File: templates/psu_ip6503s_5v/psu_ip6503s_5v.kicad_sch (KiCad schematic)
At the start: 6 parts, among them U10 IP6503S

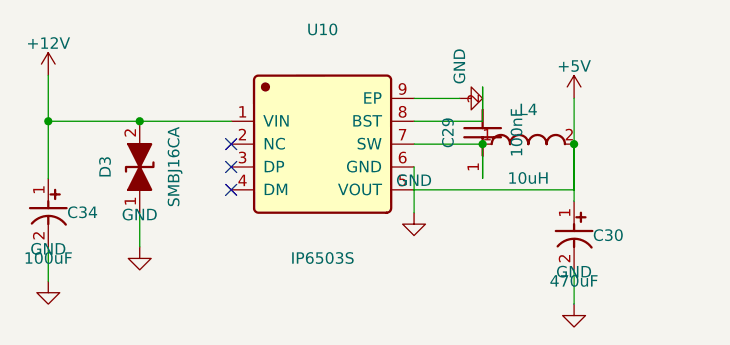
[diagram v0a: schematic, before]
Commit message: Fix IP6503S 5V PSU: upgrade output cap voltage, add ceramic decoupling
Fix #1: Replace C30 output electrolytic from 470uF 6.3V (C2891466) to
470uF 16V (Lelon VZH471M1CTR-0810, C164069). The 6.3V rating had only
26% margin on a 5V rail — now 3.2x derating for reliability.

Fix #2: Add C35 22uF 25V X5R ceramic cap (YAGEO CC1206KKX5R8BB226,
C2178233) in parallel with C30 on the output. Provides low-ESR
high-frequency decoupling for fast load transients that the electrolytic
alone cannot handle.

Both schematic and spec updated. Component count: 6 -> 7.

Co-Authored-By: Claude Opus 4.6 <noreply@anthropic.com>
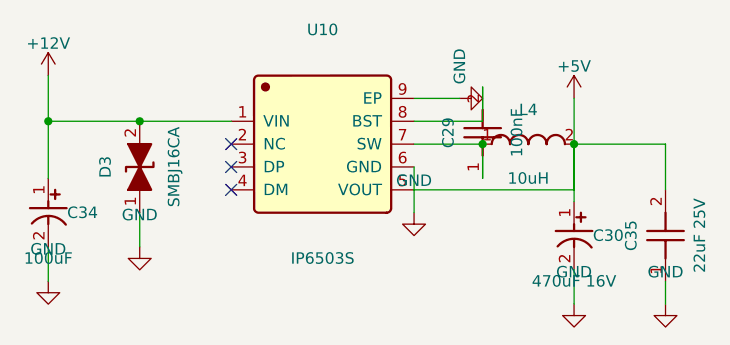
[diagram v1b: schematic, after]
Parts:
- added C35: 22uF 25V, JLCImport:CC1206KKX5R8BB226, symbol JLCImport:CC1206KKX5R8BB226
- C30: value 470uF -> 470uF 16V; footprint JLCImport:EEEFT1V681UP -> JLCImport:VZH471M1CTR-0810; symbol JLCImport:ECAP_470uF_6V3_C2891466 -> JLCImport:ECAP_470uF_16V_C164069; LCSC C2891466 -> C164069
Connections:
- net +5V: now also C35.2
- net GND: now also C35.1
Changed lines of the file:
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@@
+    (stroke (width 0) (type default))
+  )
+  (wire (pts (xy 177.8 100.33) (xy 187.96 100.33))
+    (stroke (width 0) (type default))
+  )
+  (wire (pts (xy 187.96 100.33) (xy 187.96 105.41))
+    (stroke (width 0) (type default))
+  )
+  (wire (pts (xy 187.96 115.57) (xy 187.96 118.11))
     (stroke (width 0) (type default))
   )
@@
   )
   (symbol
-    (lib_id "JLCImport:ECAP_470uF_6V3_C2891466")
+    (lib_id "JLCImport:ECAP_470uF_16V_C164069")
     (at 177.8 110.49 0)
     (unit 1)
@@
       (effects (font (size 1.27 1.27)))
     )
-    (property "Value" "470uF"
+    (property "Value" "470uF 16V"
       (at 177.8 115.57 0)
       (effects (font (size 1.27 1.27)))
     )
-    (property "Footprint" "JLCImport:EEEFT1V681UP"
+    (property "Footprint" "JLCImport:VZH471M1CTR-0810"
       (at 177.8 110.49 0)
       (effects (font (size 1.27 1.27)) hide)
     )
-    (property "LCSC" "C2891466"
+    (property "LCSC" "C164069"
       (at 177.8 110.49 0)
       (effects (font (size 1.27 1.27)) hide)
@@
           (unit 1)
         )
+      )
+    )
+  )
+  (symbol
+    (lib_id "JLCImport:CC1206KKX5R8BB226")
+    (at 187.96 110.49 90)
+    (unit 1)
+    (exclude_from_sim no)
+    (in_bom yes)
+    (on_board yes)
+    (dnp no)
+    (property "Reference" "C35"
+      (at 184.15 110.49 0)
+      (effects (font (size 1.27 1.27)))
+    )
+    (property "Value" "22uF 25V"
+      (at 191.77 110.49 0)
+      (effects (font (size 1.27 1.27)))
+    )
+    (property "Footprint" "JLCImport:CC1206KKX5R8BB226"
+      (at 187.96 110.49 0)
+      (effects (font (size 1.27 1.27)) hide)
+    )
+    (property "LCSC" "C2178233"
+      (at 187.96 110.49 0)
+      (effects (font (size 1.27 1.27)) hide)
+    )
+    (instances
+      (project "AITestProject"
+        (path "/c5e0a3b2-9d4f-6c1a-d7e5-f3a4b6c8d9e0"
+          (reference "C35")
+          (unit 1)
+        )
+      )
+    )
+  )
+  (symbol
+    (lib_id "power:GND")
+    (at 187.96 118.11 0)
+    (unit 1)
+    (exclude_from_sim no)
+    (in_bom yes)
+    (on_board yes)
+    (dnp no)
+    (property "Reference" "#PWR08"
+      (at 187.96 124.46 0)
+      (effects (font (size 1.27 1.27)) hide)
+    )
+    (property "Value" "GND"
+      (at 187.96 114.55 0)
+      (effects (font (size 1.27 1.27)))
+    )
+    (property "Footprint" ""
+      (at 187.96 118.11 0)
+      (effects (font (size 1.27 1.27)) hide)
+    )
+    (instances
+      (project "AITestProject"
+        (path "/c5e0a3b2-9d4f-6c1a-d7e5-f3a4b6c8d9e0"
+          (reference "#PWR08")
+          (unit 1)
+        )

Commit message: Add I2C pullup resistors and apply PSU audit fixes
- R33/R34: 4.22k pullups on SCL/SDA to +3.3V near ESP32
- Fix #2: C108 10uF 35V input cap for U24 3.3V converter
- Fix #3: C3 upgraded from 47uF 16V to 47uF 25V on U1 output
Applied via kicad-patch-tools (non-destructive patching)

Co-Authored-By: Claude Opus 4.6 <noreply@anthropic.com>
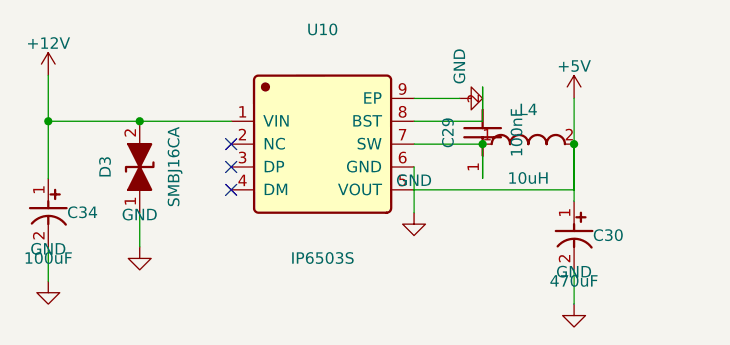
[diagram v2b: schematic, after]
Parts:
- removed C35: 22uF 25V, JLCImport:CC1206KKX5R8BB226, symbol JLCImport:CC1206KKX5R8BB226
- C30: value 470uF 16V -> 470uF; footprint JLCImport:VZH471M1CTR-0810 -> JLCImport:EEEFT1V681UP; symbol JLCImport:ECAP_470uF_16V_C164069 -> JLCImport:ECAP_470uF_6V3_C2891466; LCSC C164069 -> C2891466
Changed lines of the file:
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@@
-    (stroke (width 0) (type default))
-  )
-  (wire (pts (xy 177.8 100.33) (xy 187.96 100.33))
-    (stroke (width 0) (type default))
-  )
-  (wire (pts (xy 187.96 100.33) (xy 187.96 105.41))
-    (stroke (width 0) (type default))
-  )
-  (wire (pts (xy 187.96 115.57) (xy 187.96 118.11))
     (stroke (width 0) (type default))
   )
@@
   )
   (symbol
-    (lib_id "JLCImport:ECAP_470uF_16V_C164069")
+    (lib_id "JLCImport:ECAP_470uF_6V3_C2891466")
     (at 177.8 110.49 0)
     (unit 1)
@@
       (effects (font (size 1.27 1.27)))
     )
-    (property "Value" "470uF 16V"
+    (property "Value" "470uF"
       (at 177.8 115.57 0)
       (effects (font (size 1.27 1.27)))
     )
-    (property "Footprint" "JLCImport:VZH471M1CTR-0810"
+    (property "Footprint" "JLCImport:EEEFT1V681UP"
       (at 177.8 110.49 0)
       (effects (font (size 1.27 1.27)) hide)
     )
-    (property "LCSC" "C164069"
+    (property "LCSC" "C2891466"
       (at 177.8 110.49 0)
       (effects (font (size 1.27 1.27)) hide)
@@
           (unit 1)
         )
-      )
-    )
-  )
-  (symbol
-    (lib_id "JLCImport:CC1206KKX5R8BB226")
-    (at 187.96 110.49 90)
-    (unit 1)
-    (exclude_from_sim no)
-    (in_bom yes)
-    (on_board yes)
-    (dnp no)
-    (property "Reference" "C35"
-      (at 184.15 110.49 0)
-      (effects (font (size 1.27 1.27)))
-    )
-    (property "Value" "22uF 25V"
-      (at 191.77 110.49 0)
-      (effects (font (size 1.27 1.27)))
-    )
-    (property "Footprint" "JLCImport:CC1206KKX5R8BB226"
-      (at 187.96 110.49 0)
-      (effects (font (size 1.27 1.27)) hide)
-    )
-    (property "LCSC" "C2178233"
-      (at 187.96 110.49 0)
-      (effects (font (size 1.27 1.27)) hide)
-    )
-    (instances
-      (project "AITestProject"
-        (path "/c5e0a3b2-9d4f-6c1a-d7e5-f3a4b6c8d9e0"
-          (reference "C35")
-          (unit 1)
-        )
-      )
-    )
-  )
-  (symbol
-    (lib_id "power:GND")
-    (at 187.96 118.11 0)
-    (unit 1)
-    (exclude_from_sim no)
-    (in_bom yes)
-    (on_board yes)
-    (dnp no)
-    (property "Reference" "#PWR08"
-      (at 187.96 124.46 0)
-      (effects (font (size 1.27 1.27)) hide)
-    )
-    (property "Value" "GND"
-      (at 187.96 114.55 0)
-      (effects (font (size 1.27 1.27)))
-    )
-    (property "Footprint" ""
-      (at 187.96 118.11 0)
-      (effects (font (size 1.27 1.27)) hide)
-    )
-    (instances
-      (project "AITestProject"
-        (path "/c5e0a3b2-9d4f-6c1a-d7e5-f3a4b6c8d9e0"
-          (reference "#PWR08")
-          (unit 1)
-        )
